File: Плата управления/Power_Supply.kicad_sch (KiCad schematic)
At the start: 23 parts, among them U3 LMV324

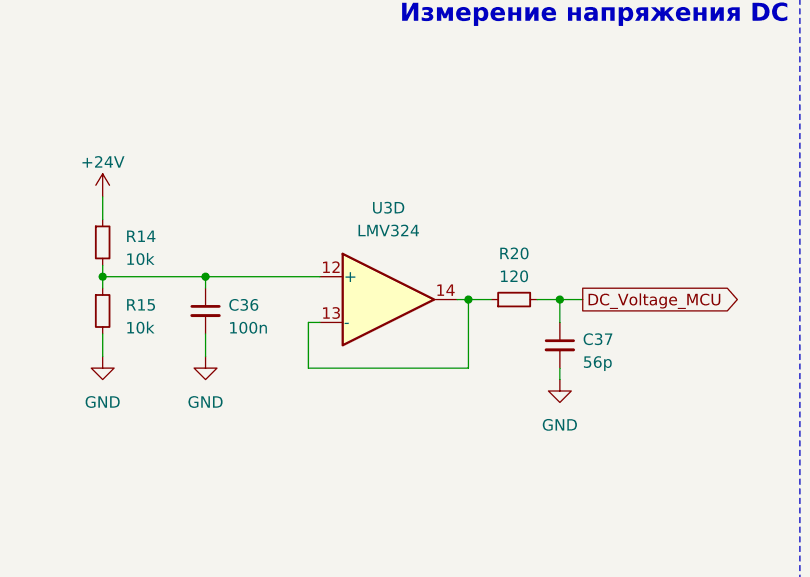
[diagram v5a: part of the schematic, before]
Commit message: Заменил разъём под силовую плату
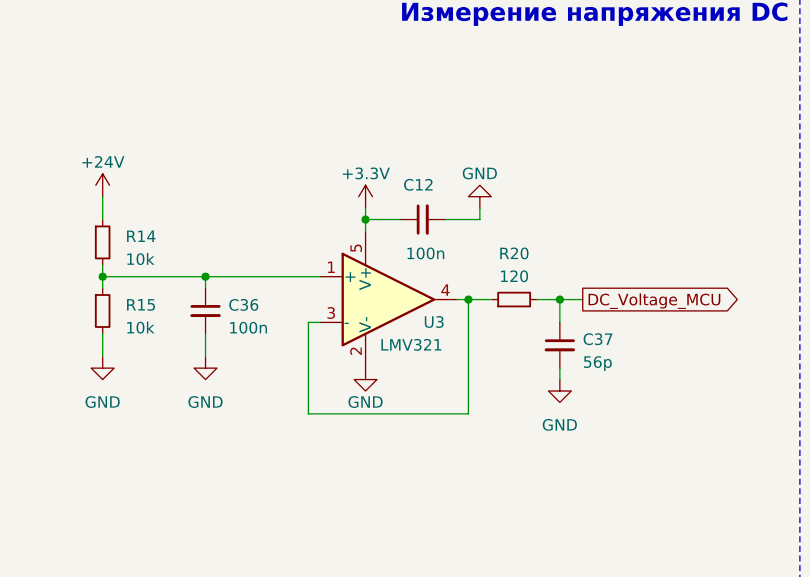
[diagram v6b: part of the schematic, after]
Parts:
- removed U3: LMV324, Package_SO:SOIC-14_3.9x8.7mm_P1.27mm, symbol Amplifier_Operational:LMV324
- added C12: 100n, Capacitor_SMD:C_0603_1608Metric_Pad1.08x0.95mm_HandSolder, symbol Device:C_Small
- added U3: LMV321, Package_TO_SOT_SMD:SOT-23-5_HandSoldering, symbol Amplifier_Operational:LMV321
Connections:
- net +3.3V: now also C12.1, U3.5 (V+)
- net GND: now also C12.2, U3.2 (V-)
- net at C36.1, R14.2, R15.1: now also U3.1 (+)
- net at R20.1: now also U3.3 (-), U3.4
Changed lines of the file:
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@@
   (junction (at 46.99 55.88) (diameter 0) (color 0 0 0 0)
+  )
+  (junction (at 165.1 45.72) (diameter 0) (color 0 0 0 0)
   )
   (junction (at 63.5 143.51) (diameter 0) (color 0 0 0 0)
@@
     (stroke (width 0) (type default))
   )
+  (wire (pts (xy 165.1 45.72) (xy 168.91 45.72))
+    (stroke (width 0) (type default))
+  )
   (wire (pts (xy 135.89 58.42) (xy 135.89 60.96))
     (stroke (width 0) (type default))
@@
     (stroke (width 0) (type default))
   )
-  (wire (pts (xy 176.53 62.23) (xy 176.53 54.61))
+  (wire (pts (xy 176.53 54.61) (xy 176.53 67.31))
     (stroke (width 0) (type default))
   )
@@
     (stroke (width 0) (type default))
   )
+  (wire (pts (xy 173.99 45.72) (xy 177.8 45.72))
+    (stroke (width 0) (type default))
+  )
   (wire (pts (xy 63.5 137.16) (xy 63.5 143.51))
     (stroke (width 0) (type default))
   )
-  (wire (pts (xy 158.75 57.15) (xy 158.75 62.23))
+  (wire (pts (xy 158.75 57.15) (xy 158.75 67.31))
     (stroke (width 0) (type default))
   )
@@
     (stroke (width 0) (type default))
   )
+  (wire (pts (xy 158.75 67.31) (xy 176.53 67.31))
+    (stroke (width 0) (type default))
+  )
   (wire (pts (xy 186.69 54.61) (xy 186.69 57.15))
     (stroke (width 0) (type default))
@@
     (stroke (width 0) (type default))
   )
+  (wire (pts (xy 165.1 45.72) (xy 165.1 46.99))
+    (stroke (width 0) (type default))
+  )
   (wire (pts (xy 53.34 143.51) (xy 53.34 123.19))
     (stroke (width 0) (type default))
@@
     (stroke (width 0) (type default))
   )
+  (wire (pts (xy 177.8 45.72) (xy 177.8 44.45))
+    (stroke (width 0) (type default))
+  )
   (wire (pts (xy 63.5 123.19) (xy 63.5 124.46))
     (stroke (width 0) (type default))
@@
     (stroke (width 0) (type default))
   )
+  (wire (pts (xy 165.1 44.45) (xy 165.1 45.72))
+    (stroke (width 0) (type default))
+  )
   (wire (pts (xy 83.82 115.57) (xy 87.63 115.57))
     (stroke (width 0) (type default))
@@
   )
   (wire (pts (xy 186.69 62.23) (xy 186.69 63.5))
-    (stroke (width 0) (type default))
-  )
-  (wire (pts (xy 158.75 62.23) (xy 176.53 62.23))
     (stroke (width 0) (type default))
   )
@@
         (path "/75f4c67c-bbde-4446-8f82-67797a1b269f/748e6803-cc54-46be-a33b-d2599b6267a4"
           (reference "R29") (unit 1)
-        )
-      )
-    )
-  )
-  (symbol (lib_id "Amplifier_Operational:LMV324") (at 167.64 54.61 0) (unit 4)
-    (in_bom yes) (on_board yes) (dnp no) (fields_autoplaced)
-    (property "Reference" "U3" (at 167.64 44.45 0)
-      (effects (font (size 1.27 1.27)))
-    )
-    (property "Value" "LMV324" (at 167.64 46.99 0)
-      (effects (font (size 1.27 1.27)))
-    )
-    (property "Footprint" "Package_SO:SOIC-14_3.9x8.7mm_P1.27mm" (at 166.37 52.07 0)
-      (effects (font (size 1.27 1.27)) hide)
-    )
-    (property "Datasheet" "http://www.ti.com/lit/ds/symlink/lmv324.pdf" (at 168.91 49.53 0)
-      (effects (font (size 1.27 1.27)) hide)
-    )
-    (pin "1")
-    (pin "2")
-    (pin "3")
-    (pin "5")
-    (pin "6")
-    (pin "7")
-    (pin "10")
-    (pin "8")
-    (pin "9")
-    (pin "12")
-    (pin "13")
-    (pin "14")
-    (pin "11")
-    (pin "4")
-    (instances
-      (project "Плата управления"
-        (path "/75f4c67c-bbde-4446-8f82-67797a1b269f/d6b8b9ce-300b-4d22-9d4c-9182eba581b1"
-          (reference "U3") (unit 4)
-        )
-        (path "/75f4c67c-bbde-4446-8f82-67797a1b269f/748e6803-cc54-46be-a33b-d2599b6267a4"
-          (reference "U3") (unit 4)
         )
       )
@@
     )
   )
+  (symbol (lib_id "power:GND") (at 177.8 44.45 180) (unit 1)
+    (in_bom yes) (on_board yes) (dnp no)
+    (property "Reference" "#PWR033" (at 177.8 38.1 0)
+      (effects (font (size 1.27 1.27)) hide)
+    )
+    (property "Value" "GND" (at 177.8 40.64 0)
+      (effects (font (size 1.27 1.27)))
+    )
+    (property "Footprint" "" (at 177.8 44.45 0)
+      (effects (font (size 1.27 1.27)) hide)
+    )
+    (property "Datasheet" "" (at 177.8 44.45 0)
+      (effects (font (size 1.27 1.27)) hide)
+    )
+    (pin "1")
+    (instances
+      (project "Плата управления"
+        (path "/75f4c67c-bbde-4446-8f82-67797a1b269f/748e6803-cc54-46be-a33b-d2599b6267a4"
+          (reference "#PWR033") (unit 1)
+        )
+      )
+    )
+  )
+  (symbol (lib_id "Amplifier_Operational:LMV321") (at 167.64 54.61 0) (unit 1)
+    (in_bom yes) (on_board yes) (dnp no)
+    (property "Reference" "U3" (at 172.72 57.15 0)
+      (effects (font (size 1.27 1.27)))
+    )
+    (property "Value" "LMV321" (at 170.18 59.69 0)
+      (effects (font (size 1.27 1.27)))
+    )
+    (property "Footprint" "Package_TO_SOT_SMD:SOT-23-5_HandSoldering" (at 167.64 54.61 0)
+      (effects (font (size 1.27 1.27)) (justify left) hide)
+    )
+    (property "Datasheet" "http://www.ti.com/lit/ds/symlink/lmv324.pdf" (at 167.64 54.61 0)
+      (effects (font (size 1.27 1.27)) hide)
+    )
+    (pin "2")
+    (pin "5")
+    (pin "1")
+    (pin "3")
+    (pin "4")
+    (instances
+      (project "Плата управления"
+        (path "/75f4c67c-bbde-4446-8f82-67797a1b269f/748e6803-cc54-46be-a33b-d2599b6267a4"
+          (reference "U3") (unit 1)
+        )
+      )
+    )
+  )
   (symbol (lib_id "Device:C_Small") (at 87.63 127 0) (unit 1)
     (in_bom yes) (on_board yes) (dnp no) (fields_autoplaced)
@@
         (path "/75f4c67c-bbde-4446-8f82-67797a1b269f/748e6803-cc54-46be-a33b-d2599b6267a4"
           (reference "#PWR093") (unit 1)
+        )
+      )
+    )
+  )
+  (symbol (lib_id "power:GND") (at 165.1 62.23 0) (unit 1)
+    (in_bom yes) (on_board yes) (dnp no)
+    (property "Reference" "#PWR031" (at 165.1 68.58 0)
+      (effects (font (size 1.27 1.27)) hide)
+    )
+    (property "Value" "GND" (at 165.1 66.04 0)
+      (effects (font (size 1.27 1.27)))
+    )
+    (property "Footprint" "" (at 165.1 62.23 0)
+      (effects (font (size 1.27 1.27)) hide)
+    )
+    (property "Datasheet" "" (at 165.1 62.23 0)
+      (effects (font (size 1.27 1.27)) hide)
+    )
+    (pin "1")
+    (instances
+      (project "Плата управления"
+        (path "/75f4c67c-bbde-4446-8f82-67797a1b269f/748e6803-cc54-46be-a33b-d2599b6267a4"
+          (reference "#PWR031") (unit 1)
+        )
+      )
+    )
+  )
+  (symbol (lib_id "power:+3.3V") (at 165.1 44.45 0) (unit 1)
+    (in_bom yes) (on_board yes) (dnp no) (fields_autoplaced)
+    (property "Reference" "#PWR032" (at 165.1 48.26 0)
+      (effects (font (size 1.27 1.27)) hide)
+    )
+    (property "Value" "+3.3V" (at 165.1 40.64 0)
+      (effects (font (size 1.27 1.27)))
+    )
+    (property "Footprint" "" (at 165.1 44.45 0)
+      (effects (font (size 1.27 1.27)) hide)
+    )
+    (property "Datasheet" "" (at 165.1 44.45 0)
+      (effects (font (size 1.27 1.27)) hide)
+    )
+    (pin "1")
+    (instances
+      (project "Плата управления"
+        (path "/75f4c67c-bbde-4446-8f82-67797a1b269f/748e6803-cc54-46be-a33b-d2599b6267a4"
+          (reference "#PWR032") (unit 1)
         )
       )
@@
         )
       )
+    )
+  )
+  (symbol (lib_id "Device:C_Small") (at 171.45 45.72 90) (unit 1)
+    (in_bom yes) (on_board yes) (dnp no)
+    (property "Reference" "C12" (at 172.72 41.91 90)
+      (effects (font (size 1.27 1.27)) (justify left))
+    )
+    (property "Value" "100n" (at 173.99 49.53 90)
+      (effects (font (size 1.27 1.27)) (justify left))
+    )
+    (property "Footprint" "Capacitor_SMD:C_0603_1608Metric_Pad1.08x0.95mm_HandSolder" (at 171.45 45.72 0)
+      (effects (font (size 1.27 1.27)) hide)
+    )
+    (property "Datasheet" "~" (at 171.45 45.72 0)
+      (effects (font (size 1.27 1.27)) hide)
+    )
+    (pin "1")
+    (pin "2")
+    (instances
+      (project "Плата управления"
+        (path "/75f4c67c-bbde-4446-8f82-67797a1b269f/748e6803-cc54-46be-a33b-d2599b6267a4"
+          (reference "C12") (unit 1)
+        )
+      )

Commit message: Редактировал схему
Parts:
- R14: value 10k -> 9.1k
- R15: value 10k -> 1k
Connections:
- net GND: now also D8.7 (PS)
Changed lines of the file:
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@@
       (effects (font (size 1.27 1.27)) (justify left))
     )
-    (property "Value" "10k" (at 138.43 57.785 0)
+    (property "Value" "1k" (at 138.43 57.785 0)
       (effects (font (size 1.27 1.27)) (justify left))
     )
@@
   (symbol (lib_id "Connverter_DCDC_My:TPS55165QPWPRQ1") (at 60.96 36.83 0) (unit 1)
     (in_bom yes) (on_board yes) (dnp no) (fields_autoplaced)
-    (property "Reference" "D8" (at 60.96 34.29 0)
-      (effects (font (size 1.27 1.27)))
-    )
-    (property "Value" "TPS55165QPWPRQ1" (at 60.96 36.83 0)
+    (property "Reference" "D8" (at 60.96 33.02 0)
+      (effects (font (size 1.27 1.27)))
+    )
+    (property "Value" "TPS55165QPWPRQ1" (at 60.96 35.56 0)
       (effects (font (size 1.27 1.27)))
     )
@@
       (effects (font (size 1.27 1.27)) (justify left))
     )
-    (property "Value" "10k" (at 138.43 50.165 0)
+    (property "Value" "9.1k" (at 138.43 50.165 0)
       (effects (font (size 1.27 1.27)) (justify left))
     )
@@
         )
       )
+    )
+  )
+  (symbol (lib_id "power:GND") (at 48.26 63.5 270) (unit 1)
+    (in_bom yes) (on_board yes) (dnp no) (fields_autoplaced)
+    (property "Reference" "#PWR061" (at 41.91 63.5 0)
+      (effects (font (size 1.27 1.27)) hide)
+    )
+    (property "Value" "GND" (at 44.45 64.135 90)
+      (effects (font (size 1.27 1.27)) (justify right))
+    )
+    (property "Footprint" "" (at 48.26 63.5 0)
+      (effects (font (size 1.27 1.27)) hide)
+    )
+    (property "Datasheet" "" (at 48.26 63.5 0)
+      (effects (font (size 1.27 1.27)) hide)
+    )
+    (pin "1")
+    (instances
+      (project "Плата управления"
+        (path "/75f4c67c-bbde-4446-8f82-67797a1b269f/748e6803-cc54-46be-a33b-d2599b6267a4"
+          (reference "#PWR061") (unit 1)
+        )
+      )

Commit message: Ещё нужно доработать
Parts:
- removed C41: 10u, Capacitor_SMD:C_1210_3225Metric_Pad1.33x2.70mm_HandSolder, symbol Device:C_Small
- removed C42: 470n, Capacitor_SMD:C_0805_2012Metric_Pad1.18x1.45mm_HandSolder, symbol Device:C_Small
- removed C44, C47, C50: 100n, Capacitor_SMD:C_0603_1608Metric_Pad1.08x0.95mm_HandSolder, symbol Device:C_Small
- removed C48: 4.7u, Capacitor_SMD:C_0805_2012Metric_Pad1.18x1.45mm_HandSolder, symbol Device:C_Small
- removed C51: 22u, Capacitor_SMD:C_1210_3225Metric_Pad1.33x2.70mm_HandSolder, symbol Device:C_Small
- removed D8: TPS55165QPWPRQ1, Package_SO:HTSSOP-20-1EP_4.4x6.5mm_P0.65mm_EP3.4x6.5mm, symbol Connverter_DCDC_My:TPS55165QPWPRQ1
- removed L2: 4.7u, Inductor_my:LQH66SN100M03L, symbol Device:L_Small
- removed R31: 100k, Resistor_SMD:R_0603_1608Metric_Pad0.98x0.95mm_HandSolder, symbol Device:R_Small
- added C18, C20, C25: 10u, Capacitor_SMD:C_1210_3225Metric_Pad1.33x2.70mm_HandSolder, symbol Device:C_Small
- added D5: MBRA320, Diode_SMD:D_SMA, symbol Device:D_Schottky_Small
- added L1: 33u, Inductor_SMD:L_10.4x10.4_H4.8, symbol Device:L_Small
- added U10: LM2594HVM-12, Package_SO:SOIC-8_3.9x4.9mm_P1.27mm, symbol Regulator_Switching:LM2594HVM-12
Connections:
- net +12V: now also C25.1, L1.2, U10.4 (FB)
- net +24V: now also C18.1, C20.1, U10.7 (VIN)
- net GND: now also C18.2, C20.2, C25.2, D5.2 (A), U10.5 (~{ON}/OFF), U10.6 (GND)
- new net: D5.1 (K), L1.1, U10.8 (OUT)
- no-connect marks 2 -> 5
